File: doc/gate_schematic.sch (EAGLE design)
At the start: 9 parts

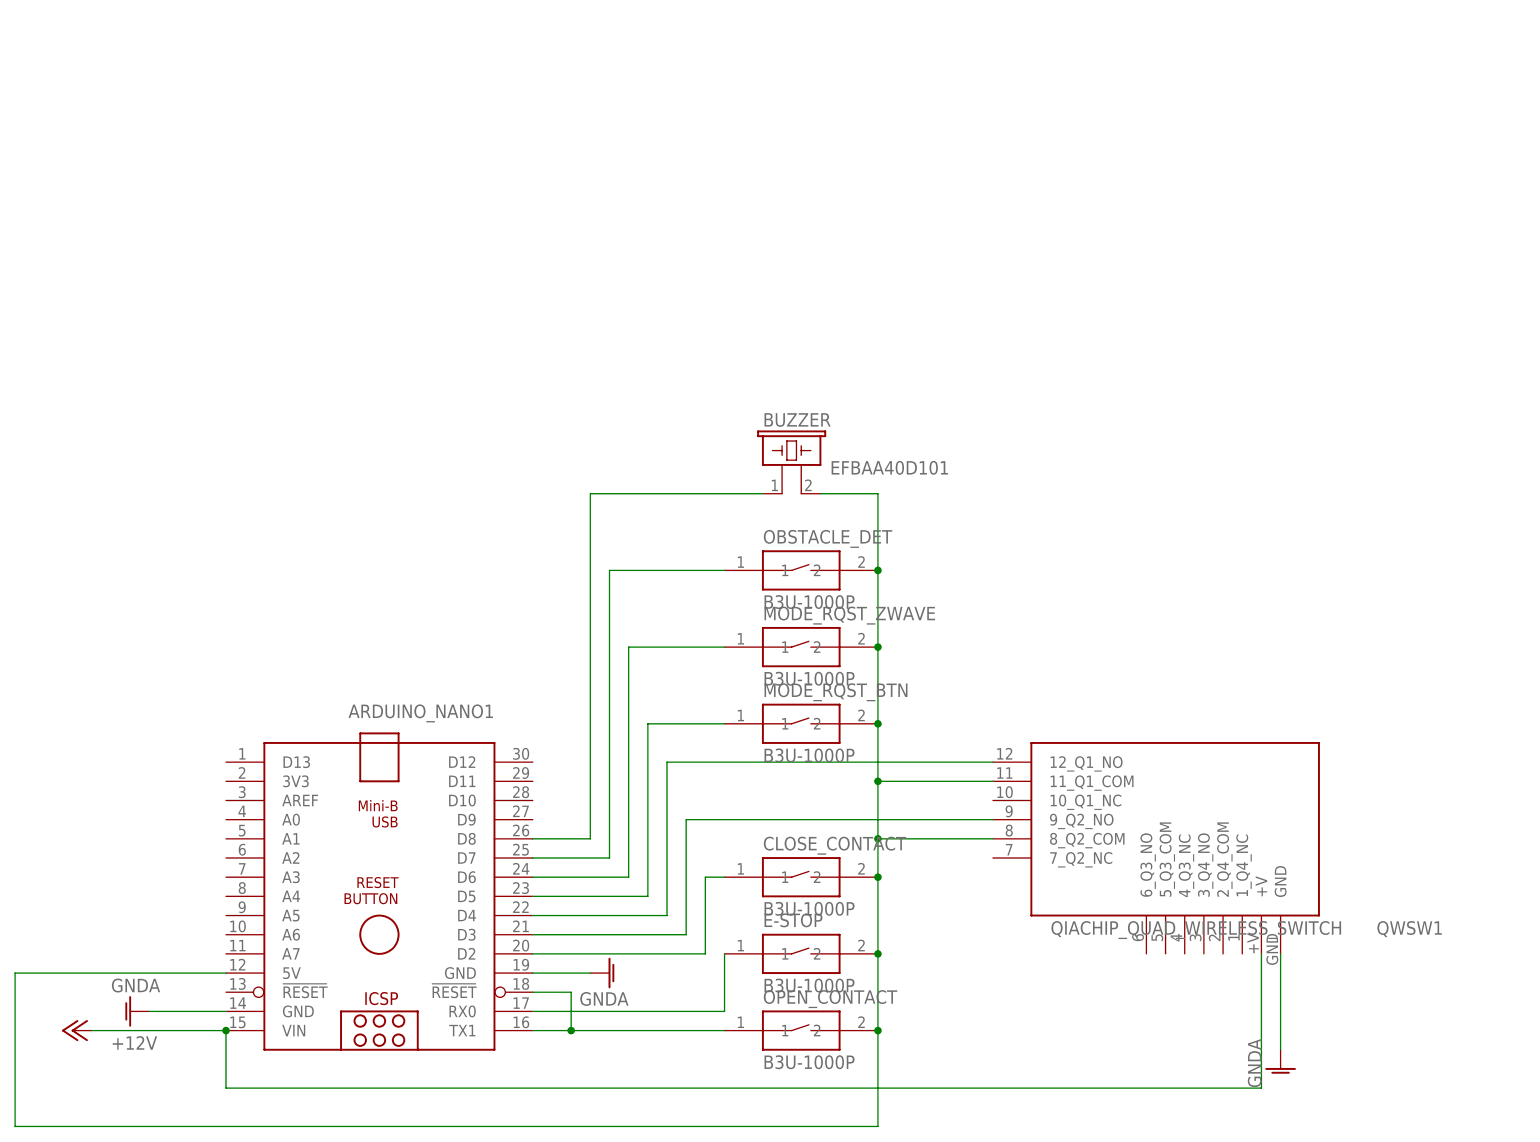
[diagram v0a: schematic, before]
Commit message: updated to detect gate position correctly
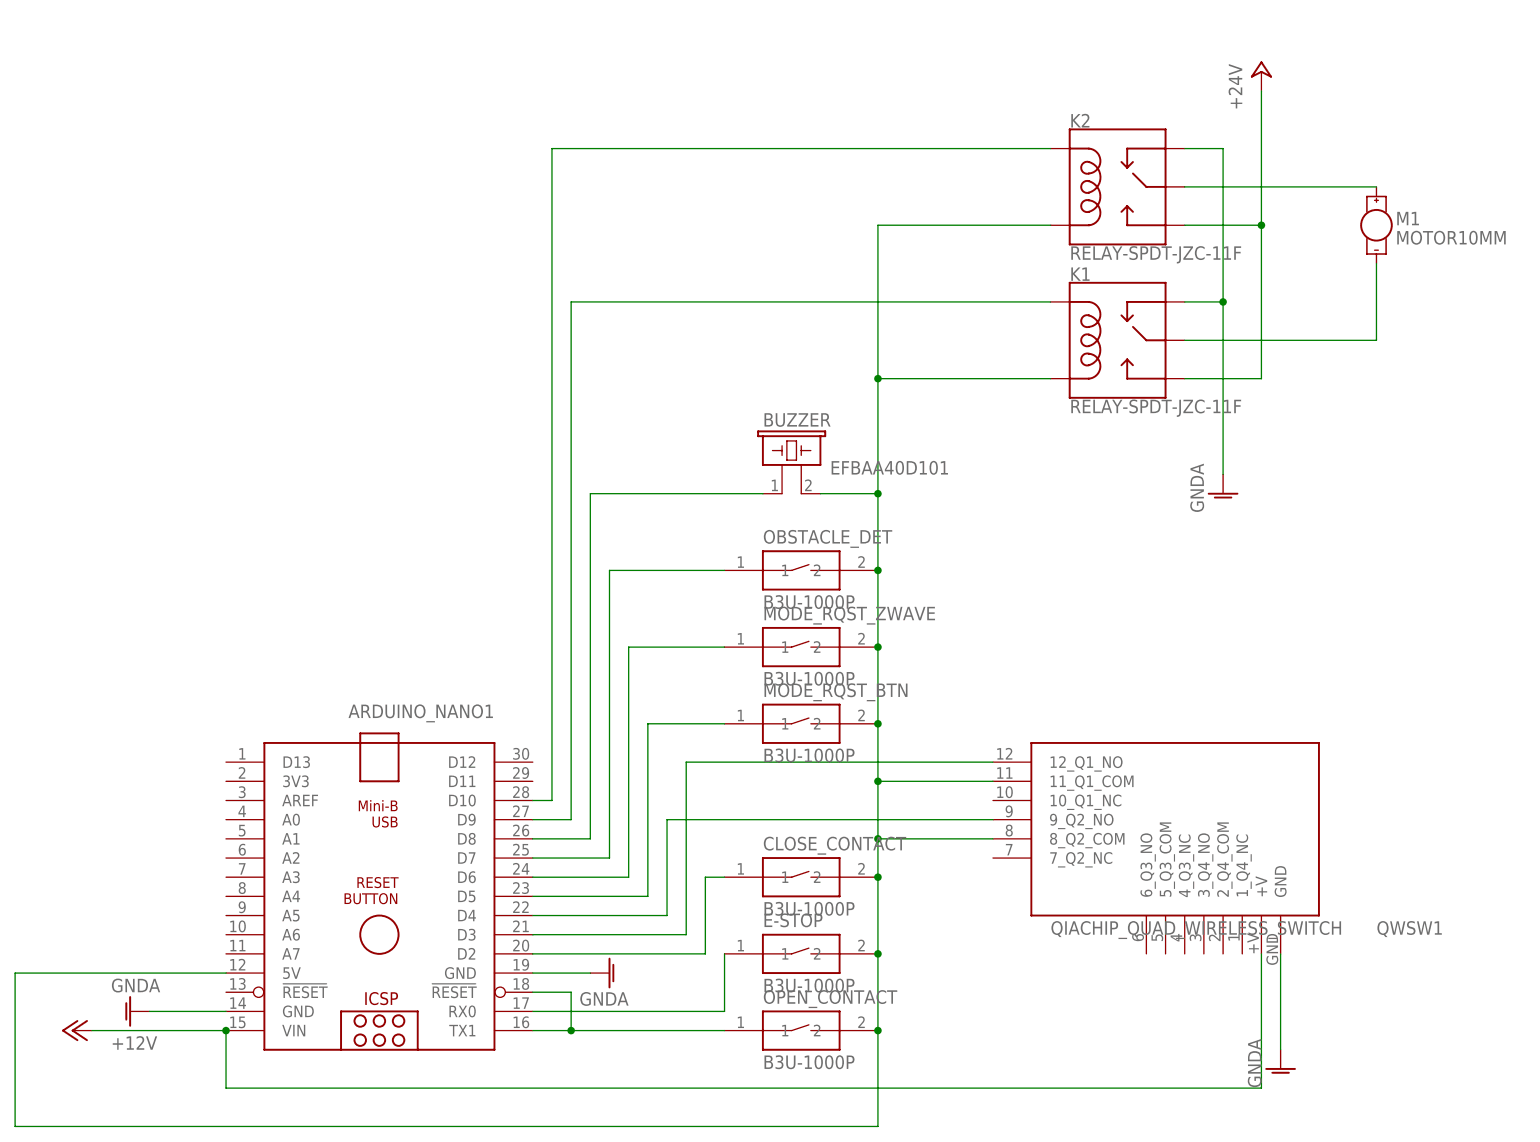
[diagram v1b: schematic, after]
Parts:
- added K1, K2: RELAY-SPDT-JZC-11F, SparkFun-Electromechanical:RELAY-SPDT-JZC-11F
- added M1: MOTOR10MM, SparkFun-Electromechanical:MOTOR10MM
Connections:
- new net +24V: K1.NO, K2.NO
- new net N$10: ARDUINO_NANO1.D10, K2.COIL1
- new net N$12: ARDUINO_NANO1.D9, K1.COIL1
- new net N$13: K1.MAIN, M1.-
- new net N$14: K2.MAIN, M1.+
- net GNDA: now also K1.NC, K2.NC
- net N$11: now also K1.COIL2, K2.COIL2
- net N$2: now also QWSW1.12_Q1_NO; no longer QWSW1.9_Q2_NO
- net N$5: now also QWSW1.9_Q2_NO; no longer QWSW1.12_Q1_NO

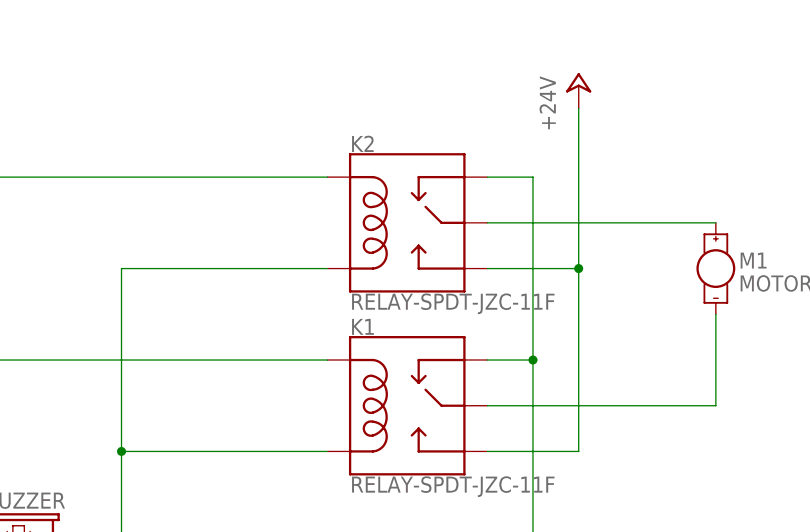
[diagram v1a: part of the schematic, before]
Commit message: interrupts won't work. nano only has 2 io interrupts
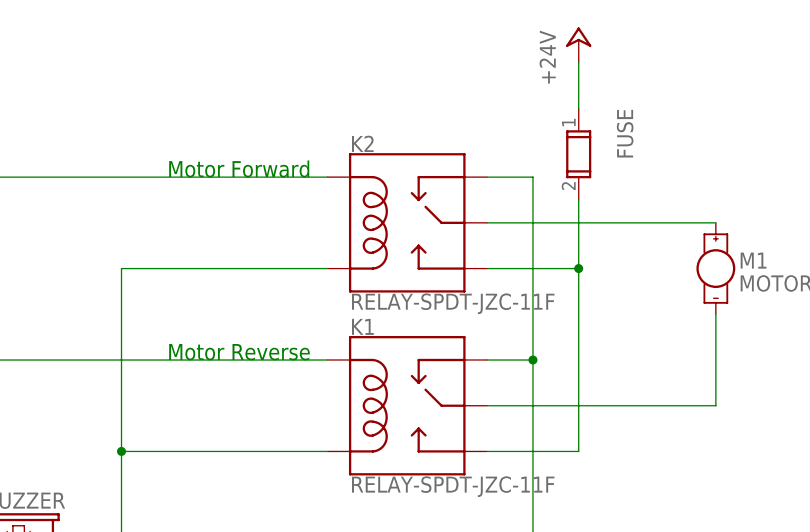
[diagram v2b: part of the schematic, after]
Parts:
- added FUSE: (no value), Wurth_Elektronik_Electromechanic_Fuse_Holder_Connectors_rev16c:696106003002
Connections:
- new net N$15: FUSE.2, K1.NO, K2.NO
- net +24V: now also FUSE.1; no longer K1.NO, K2.NO
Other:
- note added: "Motor Forward"
- note added: "Motor Reverse"
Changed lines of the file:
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@@
 <part name="GND4" library="supply1" library_urn="urn:adsk.eagle:library:371" deviceset="GNDA" device=""/>
 <part name="P+2" library="supply1" library_urn="urn:adsk.eagle:library:371" deviceset="+24V" device=""/>
+<part name="FUSE" library="Wurth_Elektronik_Electromechanic_Fuse_Holder_Connectors_rev16c" library_urn="urn:adsk.eagle:library:488577" deviceset="696106003002" device="" package3d_urn="urn:adsk.eagle:package:488595/1"/>
 </parts>
 <sheets>
 <sheet>
 <plain>
+<text x="127" y="157.48" size="1.778" layer="91">Motor Forward</text>
+<text x="127" y="137.16" size="1.778" layer="91">Motor Reverse</text>
 </plain>
 <instances>
@@
 <attribute name="VALUE" x="165.1" y="109.22" size="1.778" layer="96" rot="R90"/>
 </instance>
-<instance part="P+2" gate="1" x="172.72" y="167.64" smashed="yes">
-<attribute name="VALUE" x="170.18" y="162.56" size="1.778" layer="96" rot="R90"/>
+<instance part="P+2" gate="1" x="172.72" y="172.72" smashed="yes">
+<attribute name="VALUE" x="170.18" y="167.64" size="1.778" layer="96" rot="R90"/>
+</instance>
+<instance part="FUSE" gate="G$1" x="172.72" y="160.02" smashed="yes" rot="R270">
+<attribute name="NAME" x="176.99" y="165.1" size="1.778" layer="95" rot="R270"/>
+<attribute name="VALUE" x="166.37" y="165.1" size="1.778" layer="96" rot="R270"/>
 </instance>
 </instances>
@@
 <segment>
 <pinref part="P+2" gate="1" pin="+24V"/>
+<wire x1="172.72" y1="170.18" x2="172.72" y2="165.1" width="0.1524" layer="91"/>
+<pinref part="FUSE" gate="G$1" pin="1"/>
+</segment>
+</net>
+<net name="N$15" class="0">
+<segment>
 <pinref part="K2" gate="K$1" pin="NO"/>
-<wire x1="172.72" y1="165.1" x2="172.72" y2="147.32" width="0.1524" layer="91"/>
 <wire x1="172.72" y1="147.32" x2="162.56" y2="147.32" width="0.1524" layer="91"/>
 <pinref part="K1" gate="K$1" pin="NO"/>
@@
 <wire x1="172.72" y1="127" x2="162.56" y2="127" width="0.1524" layer="91"/>
 <junction x="172.72" y="147.32"/>
-</segment>
-</net>
+<wire x1="172.72" y1="154.94" x2="172.72" y2="147.32" width="0.1524" layer="91"/>
+<pinref part="FUSE" gate="G$1" pin="2"/>
+</segment>
+</net>
